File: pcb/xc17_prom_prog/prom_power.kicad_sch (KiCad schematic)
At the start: 126 parts, among them Q1 BC850, Q10 BC850, Q11 BC850, Q12 BC850, Q2 BC850, Q3 BC850, Q4 IRLML9301, Q5 IRLML9301, Q6 IRLML9301, Q7 IRLML9301, Q8 IRLML9301, Q9 IRLML9301, U10 LM317, U11 MC33063AD, U12 LM317, U13 LM317, U6 LM317, U7 LM317, U8 MC33063AD, U9 LM317

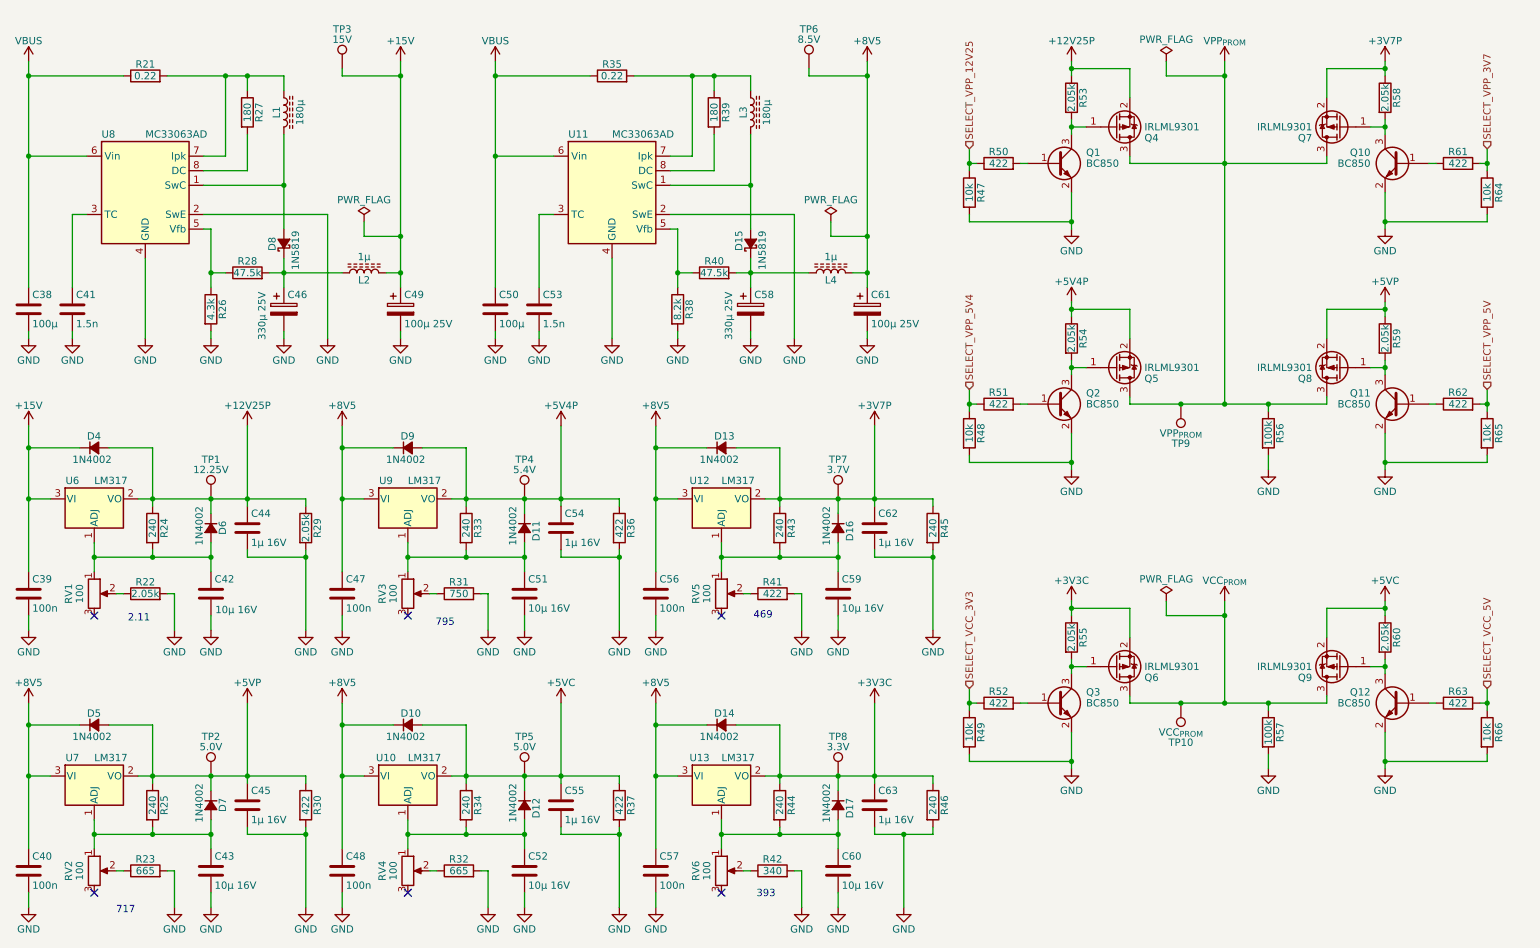
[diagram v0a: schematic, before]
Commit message: Fix MOSFETs
 * Block MOSFET body diodes by placing two MOSFETs in anti series.
 * Connect PROM LED to pin header.
 * Add transistors to actively pull PROM VCC and VPP low.
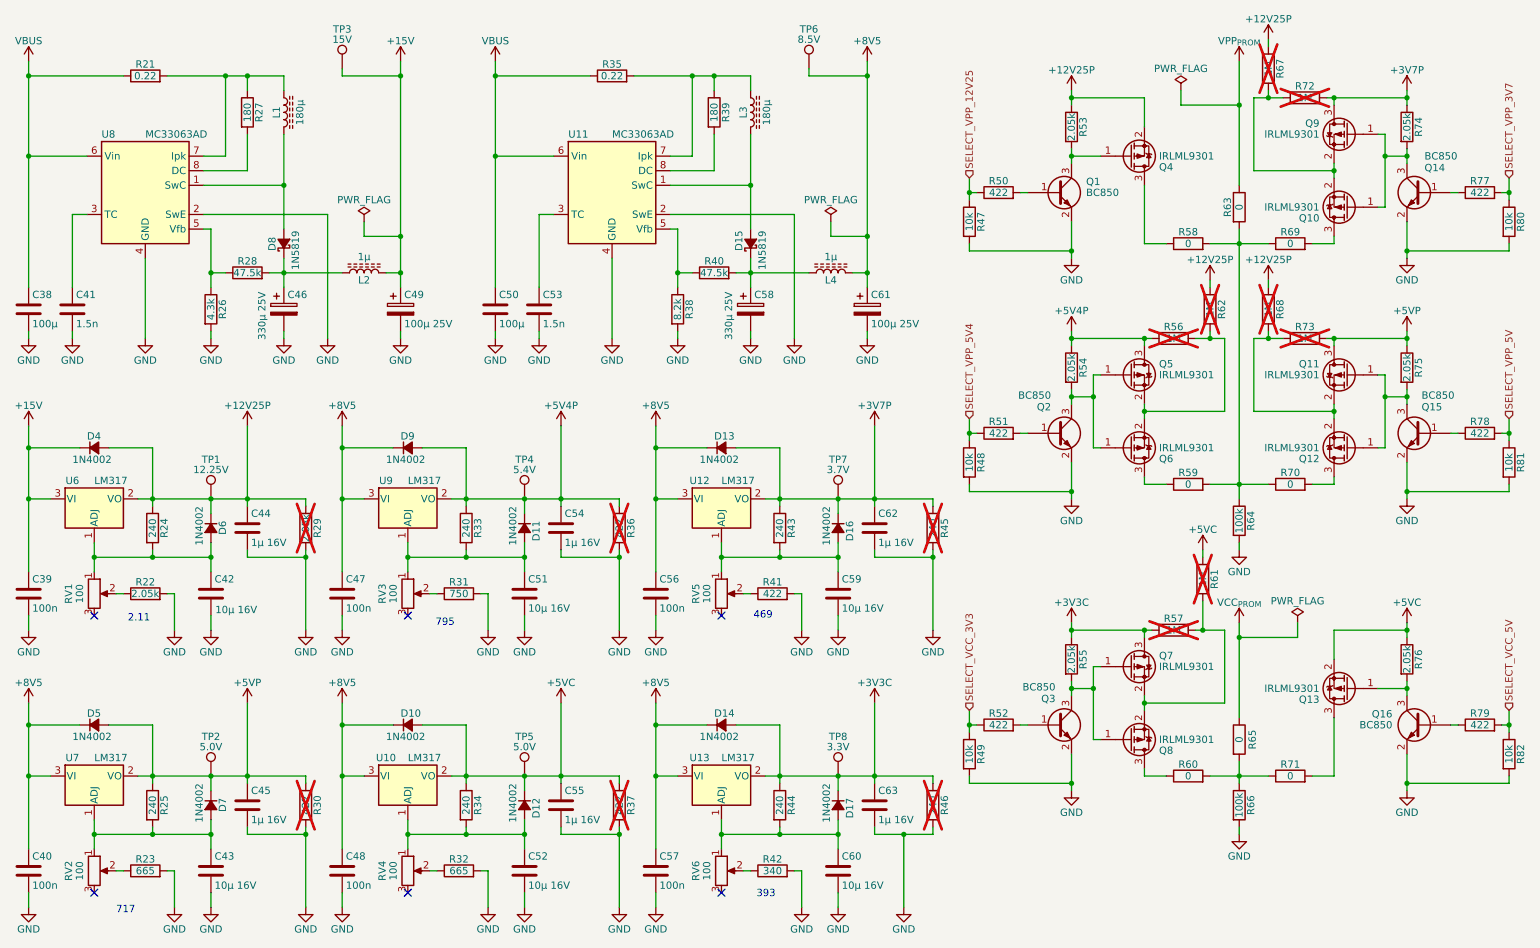
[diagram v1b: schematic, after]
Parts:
- removed TP10: VCC_{PROM}, TestPoint:TestPoint_Keystone_5010-5014_Multipurpose, symbol Connector:TestPoint
- removed TP9: VPP_{PROM}, TestPoint:TestPoint_Keystone_5010-5014_Multipurpose, symbol Connector:TestPoint
- added Q10, Q12, Q6, Q8: IRLML9301, Package_TO_SOT_SMD:SOT-23, symbol Transistor_FET:IRLML9301
- added R56, R57, R61, R62, R67, R68, R72, R73: 1M, Resistor_SMD:R_0603_1608Metric, symbol Device:R
- added R58, R59, R60, R63, R65, R69, R70, R71: 0, Resistor_SMD:R_0603_1608Metric, symbol Device:R
- R29, R30, R36, R37, R45, R46: now not fitted; now left out of the parts list
- renumbered Q8 to Q11, Q9 to Q13, Q10 to Q14, Q11 to Q15, Q12 to Q16, Q6 to Q7, Q7 to Q9, R56 to R64, R57 to R66, R58 to R74, R59 to R75, R60 to R76, R61 to R77, R62 to R78, R63 to R79, R64 to R80, R65 to R81, R66 to R82
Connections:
- net +12V25P: now also R62.1, R67.1, R68.1
- net +3V3C: now also Q7.3 (D), R57.1; no longer Q7.2 (S)
- net +3V7P: now also Q9.3 (D), R72.2; no longer Q9.2 (S)
- net +5V4P: now also Q5.3 (D), R56.1; no longer Q5.2 (S)
- net +5VC: now also R61.1
- net +5VP: now also Q11.3 (D), R73.2; no longer Q11.2 (S)
- net VCC_{PROM}: now also R65.1; no longer Q13.3 (D), Q7.3 (D), R66.1
- net VPP_{PROM}: now also R63.1; no longer Q11.3 (D), Q4.3 (D), Q5.3 (D), Q9.3 (D), R64.1
- net at Q14.3 (C), Q9.1 (G), R74.2: now also Q10.1 (G)
- net at Q2.3 (C), Q5.1 (G), R54.2: now also Q6.1 (G)
- net at Q11.1 (G), Q15.3 (C), R75.2: now also Q12.1 (G)
- net at Q3.3 (C), Q7.1 (G), R55.2: now also Q8.1 (G)
- new net: Q4.3 (D), R58.1
- new net: Q5.2 (S), Q6.2 (S), R56.2, R62.2
- new net: R60.2, R65.2, R66.1, R71.1
- new net: Q13.3 (D), R71.2
- new net: R58.2, R59.2, R63.2, R64.1, R69.1, R70.1
- new net: Q10.2 (S), Q9.2 (S), R67.2, R72.1
- new net: Q7.2 (S), Q8.2 (S), R57.2, R61.2
- new net: Q6.3 (D), R59.1
- new net: Q11.2 (S), Q12.2 (S), R68.2, R73.1
- new net: Q10.3 (D), R69.2
- new net: Q12.3 (D), R70.2
- new net: Q8.3 (D), R60.1
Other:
- moved on the sheet: Q1, Q11, Q13, Q14, Q15, Q16, Q2, Q3, Q4, Q5, Q7, Q9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
